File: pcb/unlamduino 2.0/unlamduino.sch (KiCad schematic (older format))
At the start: 49 parts, among them IC2 ATMEGA328-P, P3 CONN_01X08, U1 LM2576, U2 AP111733, Y2 16MHz

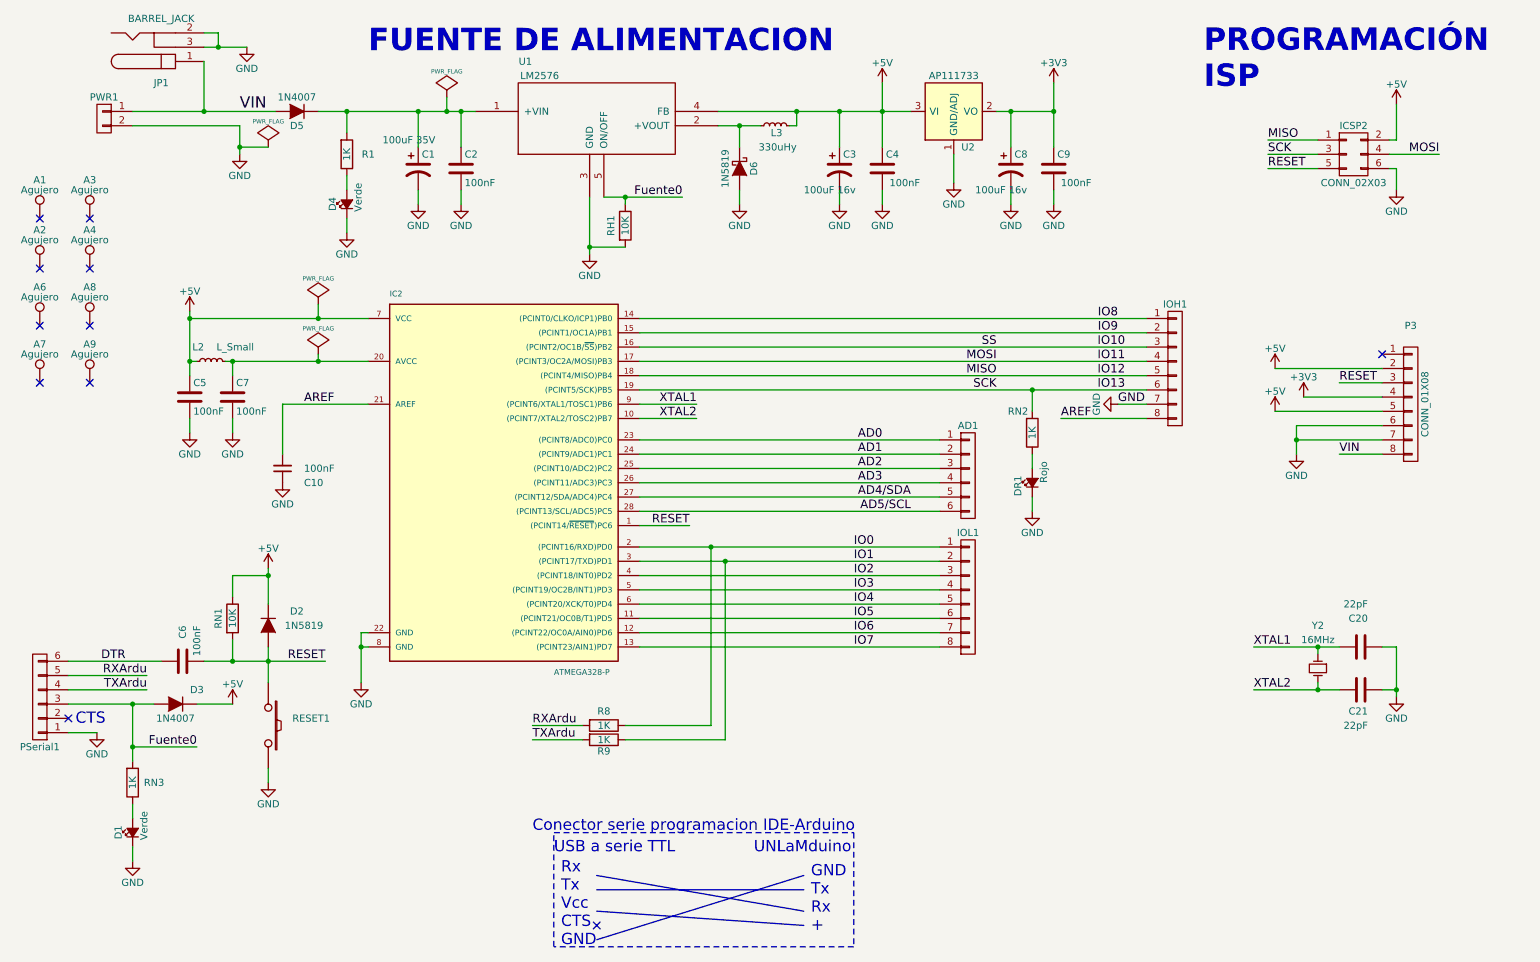
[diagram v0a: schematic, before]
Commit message: Correccion de agujeros de fijacion. Y en el esquematico conexion del adaptador USB-serie.
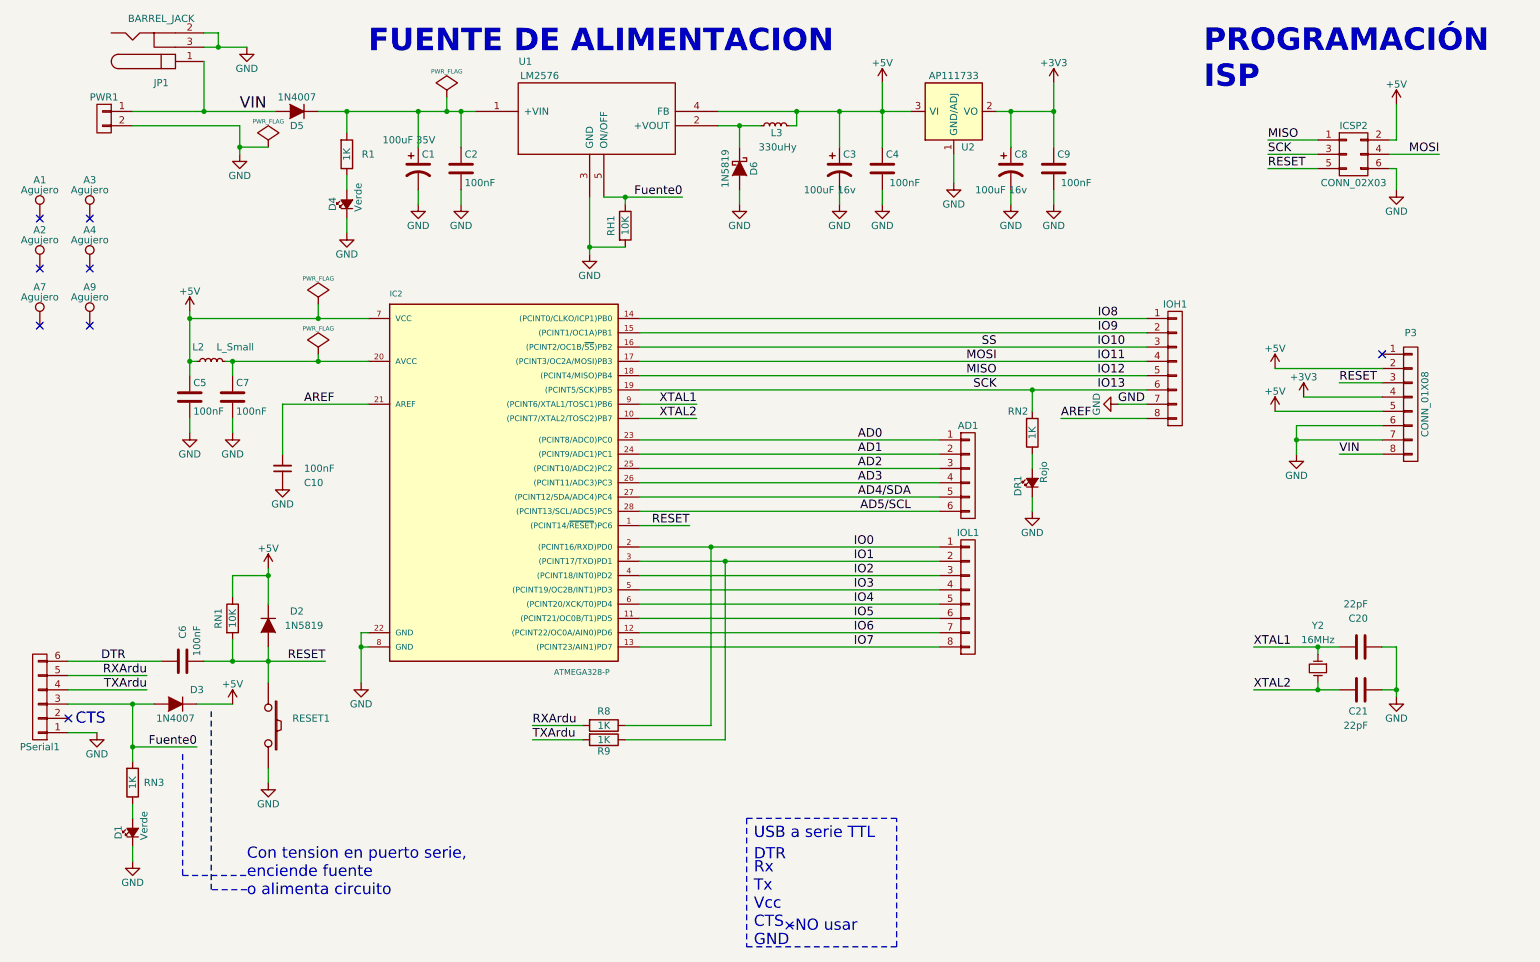
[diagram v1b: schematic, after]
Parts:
- removed A6, A8: Agujero, Mounting_Holes:MountingHole_3.2mm_M3, symbol TEST_1P
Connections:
- no-connect marks 11 -> 9
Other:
- note added: "-NO usar"
- note added: "Con tension en puerto serie,\nenciende fuente\no alimenta circuito"
- note added: "DTR"
- note removed: "Conector serie programacion IDE-Arduino"
- note removed: "GND\nTx\nRx\n+"
- note removed: "UNLaMduino"
- moved on the sheet: A7, A9
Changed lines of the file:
@@
 U 1 1 57F5793B
 P 10500 3950
-F 0 "P3" H 10500 4500 50  0000 C CNN
+F 0 "P3" H 10500 4450 50  0000 C CNN
 F 1 "CONN_01X08" V 10600 3950 50  0000 C CNN
 F 2 "Pin_Headers:Pin_Header_Straight_1x08" H 10500 3950 50  0001 C CNN
@@
 PROGRAMACIÓN\nISP
 $Comp
-L TEST_1P A8
-U 1 1 581D272E
+L TEST_1P A9
+U 1 1 581D2925
 P 1250 3400
-F 0 "A8" H 1250 3670 50  0000 C CNN
+F 0 "A9" H 1250 3670 50  0000 C CNN
 F 1 "Agujero" H 1250 3600 50  0000 C CNN
 F 2 "Mounting_Holes:MountingHole_3.2mm_M3" H 1450 3400 50  0001 C CNN
@@
 $EndComp
 $Comp
-L TEST_1P A6
-U 1 1 581D2881
+L TEST_1P A7
+U 1 1 581D2A84
 P 900 3400
-F 0 "A6" H 900 3670 50  0000 C CNN
+F 0 "A7" H 900 3670 50  0000 C CNN
 F 1 "Agujero" H 900 3600 50  0000 C CNN
 F 2 "Mounting_Holes:MountingHole_3.2mm_M3" H 1100 3400 50  0001 C CNN
 F 3 "" H 1100 3400 50  0000 C CNN
 	1    900  3400
-	1    0    0    -1
-$EndComp
-$Comp
-L TEST_1P A9
-U 1 1 581D2925
-P 1250 3800
-F 0 "A9" H 1250 4070 50  0000 C CNN
-F 1 "Agujero" H 1250 4000 50  0000 C CNN
-F 2 "Mounting_Holes:MountingHole_3.2mm_M3" H 1450 3800 50  0001 C CNN
-F 3 "" H 1450 3800 50  0000 C CNN
-	1    1250 3800
-	1    0    0    -1
-$EndComp
-$Comp
-L TEST_1P A7
-U 1 1 581D2A84
-P 900 3800
-F 0 "A7" H 900 4070 50  0000 C CNN
-F 1 "Agujero" H 900 4000 50  0000 C CNN
-F 2 "Mounting_Holes:MountingHole_3.2mm_M3" H 1100 3800 50  0001 C CNN
-F 3 "" H 1100 3800 50  0000 C CNN
-	1    900  3800
 	1    0    0    -1
 $EndComp
@@
 	2050 1900 2050 1550
 Wire Notes Line
-	4500 6950 6600 6950
-Wire Notes Line
-	6600 6950 6600 7750
-Wire Notes Line
-	6600 7750 4500 7750
-Wire Notes Line
-	4500 7750 4500 6950
-Text Notes 4500 7100 0    79   ~ 0
+	5850 6850 5850 7750
+Text Notes 5900 7000 0    79   ~ 0
 USB a serie TTL
-Text Notes 4550 7750 0    79   ~ 0
-Rx\nTx\nVcc\nCTS\nGND
-Text Notes 6300 7650 0    79   ~ 0
-GND\nTx\nRx\n+
-Wire Bus Line
-	4800 7250 6250 7500
-Wire Bus Line
-	4800 7350 6250 7350
-Wire Bus Line
-	4800 7700 6250 7250
-Wire Bus Line
-	6250 7600 4800 7500
-NoConn ~ 4800 7600
-Text Notes 5900 7100 0    79   ~ 0
-UNLaMduino
-Text Notes 4350 6950 0    79   ~ 0
-Conector serie programacion IDE-Arduino
+NoConn ~ 6150 7600
 $Comp
 L CONN_01X08 IOH1
@@
 $EndComp
 NoConn ~ 1250 3400
-NoConn ~ 1250 3800
 NoConn ~ 900  3400
-NoConn ~ 900  3800
+Text Notes 5900 7750 0    79   ~ 0
+Rx\nTx\nVcc\nCTS\nGND
+Wire Notes Line
+	5850 6850 6900 6850
+Wire Notes Line
+	5850 7750 6900 7750
+Text Notes 6150 7650 0    79   ~ 0
+-NO usar
+Text Notes 5900 7150 0    79   ~ 0
+DTR
+Wire Notes Line
+	6900 7750 6900 6850
+Text Notes 2350 7400 0    79   ~ 0
+Con tension en puerto serie,\nenciende fuente\no alimenta circuito
+Wire Notes Line
+	2350 7350 2100 7350
+Wire Notes Line
+	2100 7350 2100 6100
+Wire Notes Line
+	1900 6400 1900 7250
+Wire Notes Line
+	1900 7250 2350 7250
 $EndSCHEMATC
